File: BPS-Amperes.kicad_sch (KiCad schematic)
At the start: 37 parts, among them J1 Conn_02x10_Odd_Even, J2 ShuntConn, U1 INA186A3IDDFT, U2 OPA2196, U3 LTC2315, U4 REF1930AIDDCT

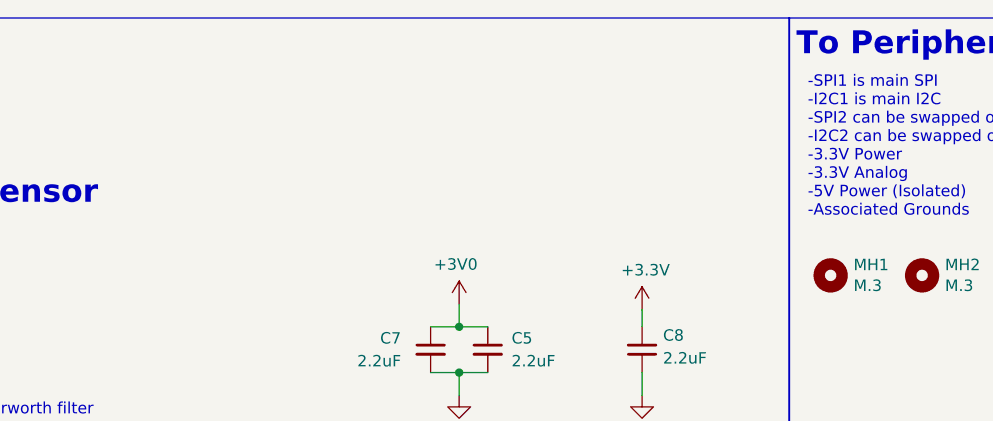
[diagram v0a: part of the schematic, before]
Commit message: Added Shunt Passthrough & Test Conns
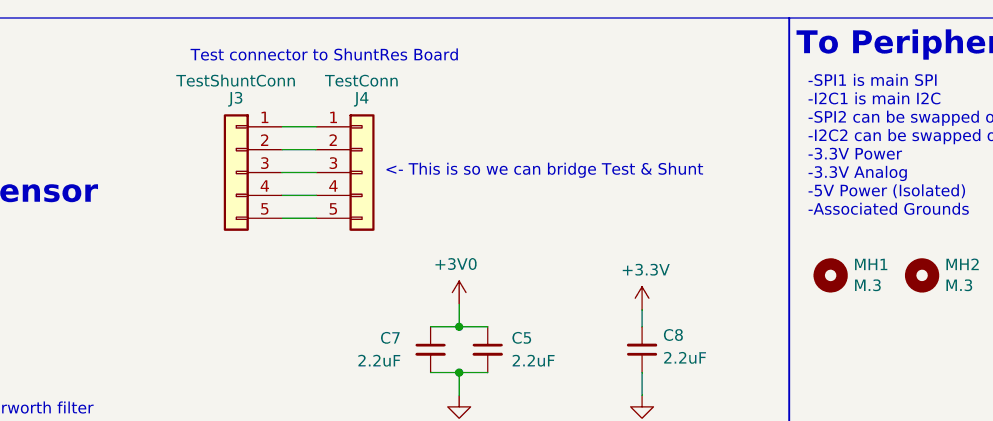
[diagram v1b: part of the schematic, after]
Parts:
- added J3: TestShuntConn, Connector_PinSocket_2.54mm:PinSocket_1x05_P2.54mm_Vertical, symbol Connector_Generic:Conn_01x05
- added J4: TestConn, Connector_PinSocket_2.54mm:PinSocket_1x05_P2.54mm_Horizontal, symbol Connector_Generic:Conn_01x05
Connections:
- new net: J3.1 (Pin_1), J4.1 (Pin_1)
- new net: J3.2 (Pin_2), J4.2 (Pin_2)
- new net: J3.3 (Pin_3), J4.3 (Pin_3)
- new net: J3.4 (Pin_4), J4.4 (Pin_4)
- new net: J3.5 (Pin_5), J4.5 (Pin_5)
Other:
- note added: "<- This is so we can bridge Test & Shunt"
- note added: "Test connector to ShuntRes Board"
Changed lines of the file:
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@@
+    (stroke (width 0) (type default))
+  )
+  (wire (pts (xy 120.65 26.67) (xy 124.46 26.67))
     (stroke (width 0) (type default))
   )
@@
     (stroke (width 0) (type default))
   )
+  (wire (pts (xy 120.65 31.75) (xy 124.46 31.75))
+    (stroke (width 0) (type default))
+  )
   (wire (pts (xy 122.555 78.74) (xy 123.825 78.74))
     (stroke (width 0) (type default))
@@
     (stroke (width 0) (type default))
   )
+  (wire (pts (xy 120.65 34.29) (xy 124.46 34.29))
+    (stroke (width 0) (type default))
+  )
   (wire (pts (xy 226.06 35.56) (xy 224.155 35.56))
     (stroke (width 0) (type default))
@@
     (stroke (width 0) (type default))
   )
+  (wire (pts (xy 120.65 24.13) (xy 124.46 24.13))
+    (stroke (width 0) (type default))
+  )
   (wire (pts (xy 238.125 30.48) (xy 241.3 30.48))
     (stroke (width 0) (type default))
@@
   )
   (wire (pts (xy 278.13 38.1) (xy 280.035 38.1))
+    (stroke (width 0) (type default))
+  )
+  (wire (pts (xy 120.65 29.21) (xy 124.46 29.21))
     (stroke (width 0) (type default))
   )
@@
   (text "To Peripheral SOM" (at 177.8 16.51 0)
     (effects (font (size 2.54 2.54) (thickness 0.508) bold) (justify left bottom))
+  )
+  (text "Test connector to ShuntRes Board" (at 110.49 17.145 0)
+    (effects (font (size 1.27 1.27)) (justify left bottom))
   )
   (text "Current shunt resistor (100u ohms) and thermistor (PT1000) will\nbe placed on a separate PCB located closer to the battery. "
@@
   (text "Daughterboard Features" (at 12.7 16.51 0)
     (effects (font (size 2.54 2.54) (thickness 0.508) bold) (justify left bottom))
+  )
+  (text "<- This is so we can bridge Test & Shunt" (at 132.08 29.845 0)
+    (effects (font (size 1.27 1.27)) (justify left bottom))
   )
   (text "-SPI1 is main SPI\n-I2C1 is main I2C\n-SPI2 can be swapped out for 4xGPIO\n-I2C2 can be swapped out for 2xGPIO\n-3.3V Power\n-3.3V Analog\n-5V Power (Isolated)\n-Associated Grounds"
@@
     )
   )
+  (symbol (lib_id "Connector_Generic:Conn_01x05") (at 129.54 29.21 0) (unit 1)
+    (in_bom yes) (on_board yes) (dnp no)
+    (property "Reference" "J4" (at 129.54 20.955 0)
+      (effects (font (size 1.27 1.27)))
+    )
+    (property "Value" "TestConn" (at 129.54 19.05 0)
+      (effects (font (size 1.27 1.27)))
+    )
+    (property "Footprint" "Connector_PinSocket_2.54mm:PinSocket_1x05_P2.54mm_Horizontal" (at 129.54 29.21 0)
+      (effects (font (size 1.27 1.27)) hide)
+    )
+    (property "Datasheet" "~" (at 129.54 29.21 0)
+      (effects (font (size 1.27 1.27)) hide)
+    )
+    (pin "1")
+    (pin "2")
+    (pin "3")
+    (pin "4")
+    (pin "5")
+    (instances
+      (project "BPS-Amperes"
+        (path "/637f68f0-cb9c-412a-8573-5d8e7ef6d8a2"
+          (reference "J4") (unit 1)
+        )
+      )
+      (project "BPS-Amperes"
+        (path "/e63e39d7-6ac0-4ffd-8aa3-1841a4541b55"
+          (reference "J1") (unit 1)
+        )
+      )
+    )
+  )
   (symbol (lib_id "Connector_Generic:Conn_01x05") (at 22.225 43.18 0) (mirror y) (unit 1)
     (in_bom yes) (on_board yes) (dnp no)
@@
         )
       )
+    )
+  )
+  (symbol (lib_id "Connector_Generic:Conn_01x05") (at 115.57 29.21 0) (mirror y) (unit 1)
+    (in_bom yes) (on_board yes) (dnp no)
+    (property "Reference" "J3" (at 115.57 20.955 0)
+      (effects (font (size 1.27 1.27)))
+    )
+    (property "Value" "TestShuntConn" (at 115.57 19.05 0)
+      (effects (font (size 1.27 1.27)))
+    )
+    (property "Footprint" "Connector_PinSocket_2.54mm:PinSocket_1x05_P2.54mm_Vertical" (at 115.57 29.21 0)
+      (effects (font (size 1.27 1.27)) hide)
+    )
+    (property "Datasheet" "~" (at 115.57 29.21 0)
+      (effects (font (size 1.27 1.27)) hide)
+    )
+    (pin "1")
+    (pin "2")
+    (pin "3")
+    (pin "4")
+    (pin "5")
+    (instances
+      (project "BPS-Amperes"
+        (path "/637f68f0-cb9c-412a-8573-5d8e7ef6d8a2"
+          (reference "J3") (unit 1)
+        )
+      )
+      (project "BPS-Amperes"
+        (path "/e63e39d7-6ac0-4ffd-8aa3-1841a4541b55"
+          (reference "J1") (unit 1)
+        )
+      )

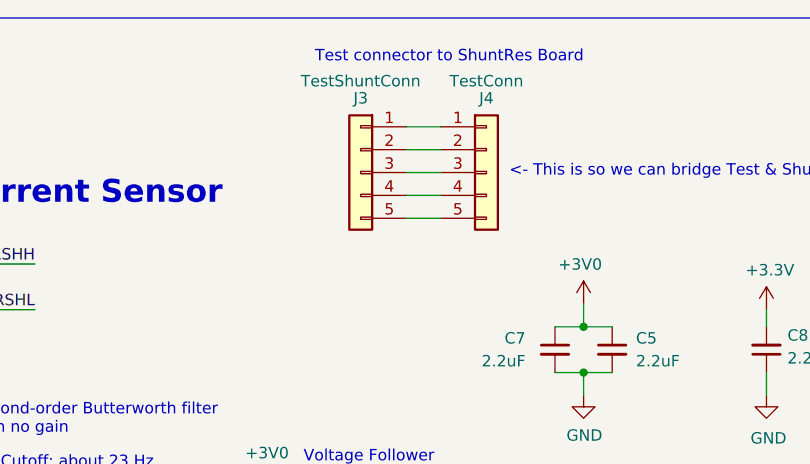
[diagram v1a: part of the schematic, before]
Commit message: Added Mounting Holes to RShunt Board
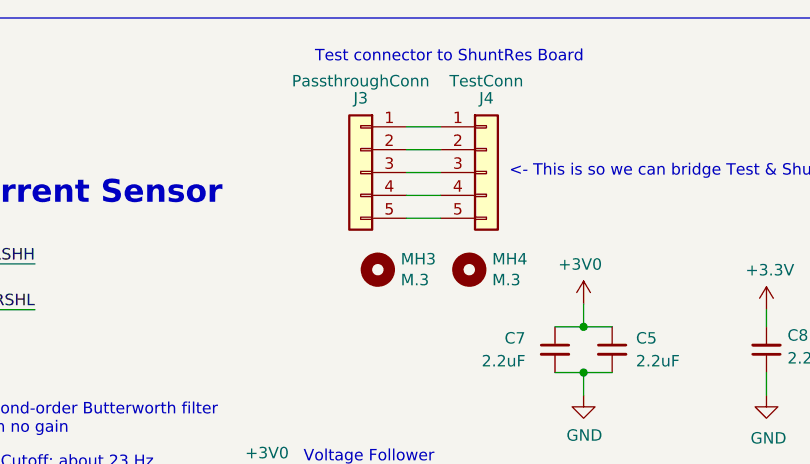
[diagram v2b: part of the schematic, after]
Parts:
- added MH3, MH4: M.3, MountingHole:MountingHole_2.7mm_M2.5, symbol Mechanical:MountingHole
- J3: value TestShuntConn -> PassthroughConn
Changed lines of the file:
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@@
+    )
+  )
+  (symbol (lib_id "Mechanical:MountingHole") (at 127.635 40.005 0) (unit 1)
+    (in_bom yes) (on_board yes) (dnp no)
+    (property "Reference" "MH4" (at 130.175 38.8366 0)
+      (effects (font (size 1.27 1.27)) (justify left))
+    )
+    (property "Value" "M.3" (at 130.175 41.148 0)
+      (effects (font (size 1.27 1.27)) (justify left))
+    )
+    (property "Footprint" "MountingHole:MountingHole_2.7mm_M2.5" (at 127.635 40.005 0)
+      (effects (font (size 1.27 1.27)) hide)
+    )
+    (property "Datasheet" "~" (at 127.635 40.005 0)
+      (effects (font (size 1.27 1.27)) hide)
+    )
+    (instances
+      (project "BPS-Amperes"
+        (path "/637f68f0-cb9c-412a-8573-5d8e7ef6d8a2"
+          (reference "MH4") (unit 1)
+        )
+      )
+      (project "BPS-Leader"
+        (path "/c248b171-df31-4e8a-afb6-607fa2df334b"
+          (reference "MH2") (unit 1)
+        )
+      )
+      (project "BPS-PeripheralSOM"
+        (path "/d5ebd247-5a7c-47c2-8aee-beabaef72d6d"
+          (reference "MH2") (unit 1)
+        )
+      )
     )
   )
@@
     )
   )
+  (symbol (lib_id "Mechanical:MountingHole") (at 117.475 40.005 0) (unit 1)
+    (in_bom yes) (on_board yes) (dnp no)
+    (property "Reference" "MH3" (at 120.015 38.8366 0)
+      (effects (font (size 1.27 1.27)) (justify left))
+    )
+    (property "Value" "M.3" (at 120.015 41.148 0)
+      (effects (font (size 1.27 1.27)) (justify left))
+    )
+    (property "Footprint" "MountingHole:MountingHole_2.7mm_M2.5" (at 117.475 40.005 0)
+      (effects (font (size 1.27 1.27)) hide)
+    )
+    (property "Datasheet" "~" (at 117.475 40.005 0)
+      (effects (font (size 1.27 1.27)) hide)
+    )
+    (instances
+      (project "BPS-Amperes"
+        (path "/637f68f0-cb9c-412a-8573-5d8e7ef6d8a2"
+          (reference "MH3") (unit 1)
+        )
+      )
+      (project "BPS-Leader"
+        (path "/c248b171-df31-4e8a-afb6-607fa2df334b"
+          (reference "MH1") (unit 1)
+        )
+      )
+      (project "BPS-PeripheralSOM"
+        (path "/d5ebd247-5a7c-47c2-8aee-beabaef72d6d"
+          (reference "MH1") (unit 1)
+        )
+      )
+    )
+  )
   (symbol (lib_id "Device:C_Small") (at 69.215 69.85 180) (unit 1)
     (in_bom yes) (on_board yes) (dnp no)
@@
       (effects (font (size 1.27 1.27)))
     )
-    (property "Value" "TestShuntConn" (at 115.57 19.05 0)
-      (effects (font (size 1.27 1.27)))
-    )
+    (property "Value" "PassthroughConn" (at 115.57 19.05 0)
+      (effects (font (size 1.27 1.27)))
+    )

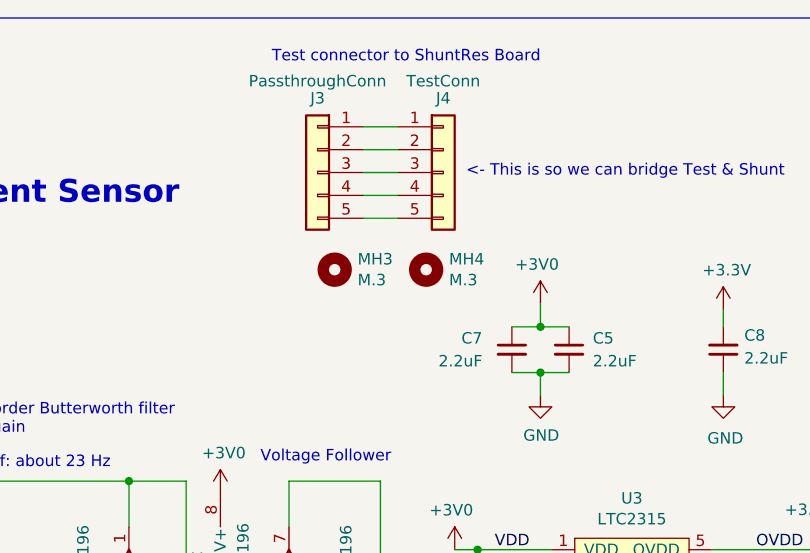
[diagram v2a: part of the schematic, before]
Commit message: Sike we don't need mounting holes
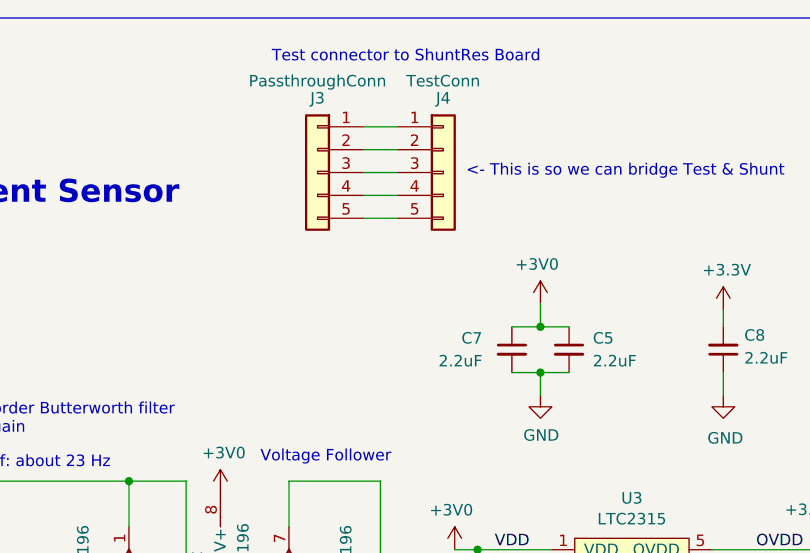
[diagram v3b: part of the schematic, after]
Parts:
- removed MH3, MH4: M.3, MountingHole:MountingHole_2.7mm_M2.5, symbol Mechanical:MountingHole
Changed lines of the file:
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@@
-    )
-  )
-  (symbol (lib_id "Mechanical:MountingHole") (at 127.635 40.005 0) (unit 1)
-    (in_bom yes) (on_board yes) (dnp no)
-    (property "Reference" "MH4" (at 130.175 38.8366 0)
-      (effects (font (size 1.27 1.27)) (justify left))
-    )
-    (property "Value" "M.3" (at 130.175 41.148 0)
-      (effects (font (size 1.27 1.27)) (justify left))
-    )
-    (property "Footprint" "MountingHole:MountingHole_2.7mm_M2.5" (at 127.635 40.005 0)
-      (effects (font (size 1.27 1.27)) hide)
-    )
-    (property "Datasheet" "~" (at 127.635 40.005 0)
-      (effects (font (size 1.27 1.27)) hide)
-    )
-    (instances
-      (project "BPS-Amperes"
-        (path "/637f68f0-cb9c-412a-8573-5d8e7ef6d8a2"
-          (reference "MH4") (unit 1)
-        )
-      )
-      (project "BPS-Leader"
-        (path "/c248b171-df31-4e8a-afb6-607fa2df334b"
-          (reference "MH2") (unit 1)
-        )
-      )
-      (project "BPS-PeripheralSOM"
-        (path "/d5ebd247-5a7c-47c2-8aee-beabaef72d6d"
-          (reference "MH2") (unit 1)
-        )
-      )
     )
   )
@@
         )
       )
-    )
-  )
-  (symbol (lib_id "Mechanical:MountingHole") (at 117.475 40.005 0) (unit 1)
-    (in_bom yes) (on_board yes) (dnp no)
-    (property "Reference" "MH3" (at 120.015 38.8366 0)
-      (effects (font (size 1.27 1.27)) (justify left))
-    )
-    (property "Value" "M.3" (at 120.015 41.148 0)
-      (effects (font (size 1.27 1.27)) (justify left))
-    )
-    (property "Footprint" "MountingHole:MountingHole_2.7mm_M2.5" (at 117.475 40.005 0)
-      (effects (font (size 1.27 1.27)) hide)
-    )
-    (property "Datasheet" "~" (at 117.475 40.005 0)
-      (effects (font (size 1.27 1.27)) hide)
-    )
-    (instances
-      (project "BPS-Amperes"
-        (path "/637f68f0-cb9c-412a-8573-5d8e7ef6d8a2"
-          (reference "MH3") (unit 1)
-        )
-      )
-      (project "BPS-Leader"
-        (path "/c248b171-df31-4e8a-afb6-607fa2df334b"
-          (reference "MH1") (unit 1)
-        )
-      )
-      (project "BPS-PeripheralSOM"
-        (path "/d5ebd247-5a7c-47c2-8aee-beabaef72d6d"
-          (reference "MH1") (unit 1)
-        )
-      )

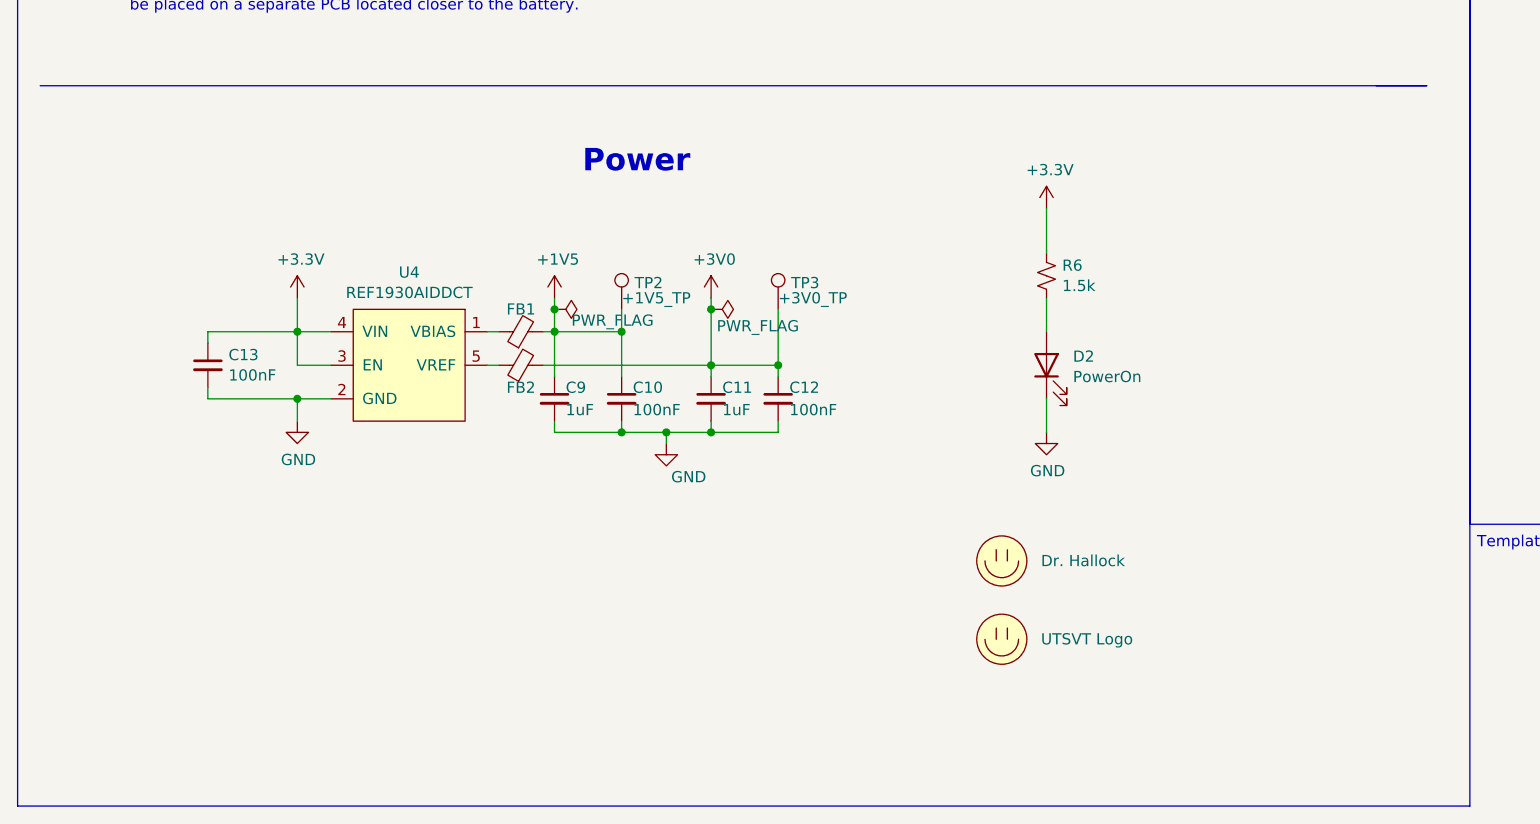
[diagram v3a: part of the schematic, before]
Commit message: Changed testpoints and arranged power components
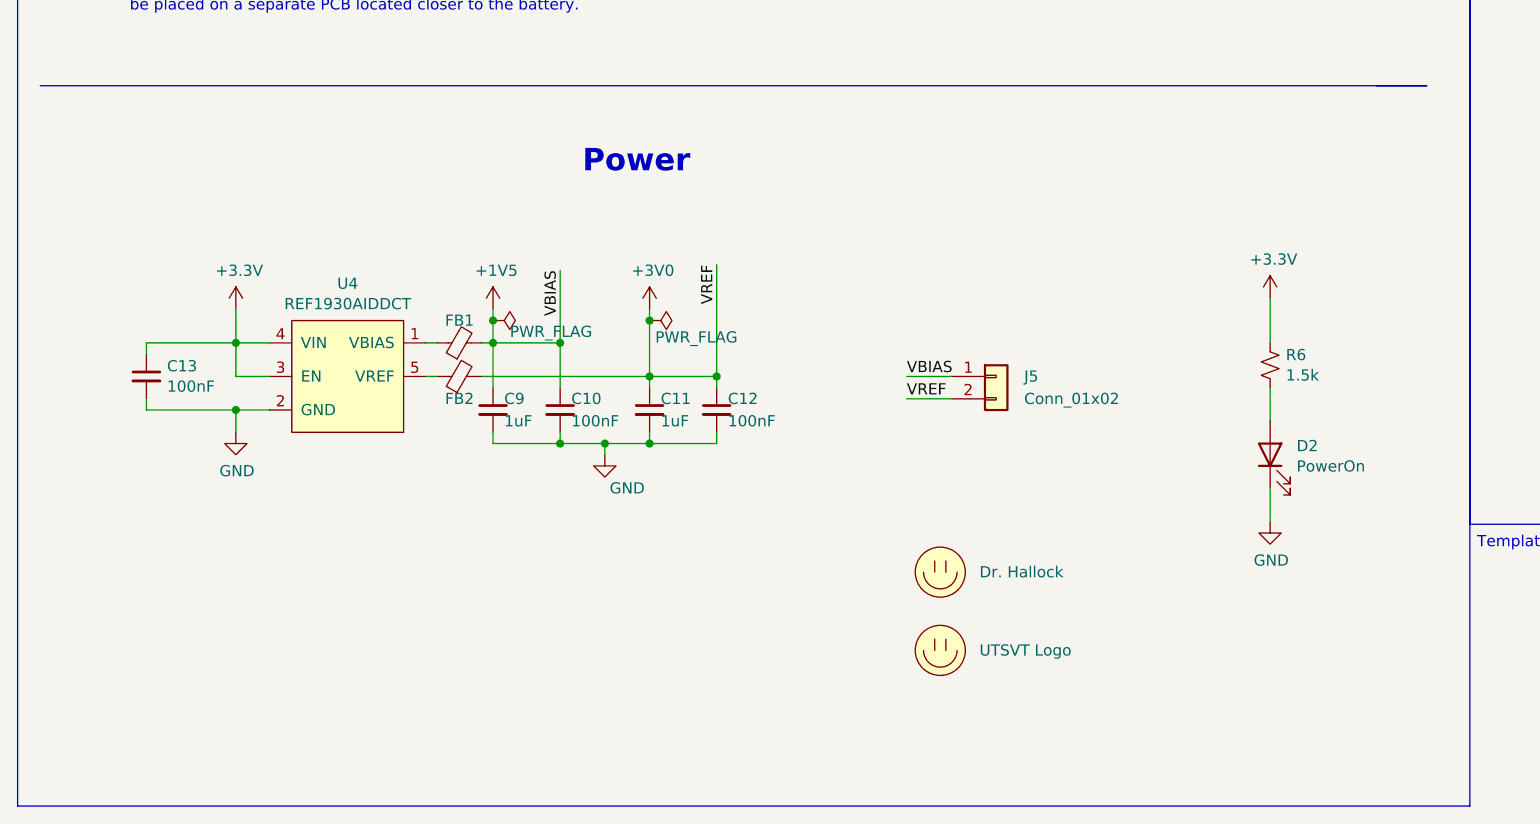
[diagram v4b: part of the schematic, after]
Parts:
- removed TP2: +1V5_TP, TestPoint:TestPoint_Pad_1.5x1.5mm, symbol Connector:TestPoint
- removed TP3: +3V0_TP, TestPoint:TestPoint_Pad_1.5x1.5mm, symbol Connector:TestPoint
- added J5: Conn_01x02, Connector_PinSocket_2.54mm:PinSocket_1x02_P2.54mm_Horizontal, symbol Connector_Generic:Conn_01x02
- TP1: footprint Connector_PinSocket_2.54mm:PinSocket_1x01_P2.54mm_Vertical -> Connector_PinSocket_2.54mm:PinSocket_1x01_P2.54mm_Horizontal
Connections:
- net +1V5: now also J5.1 (Pin_1)
- net +3V0: now also J5.2 (Pin_2)
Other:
- moved on the sheet: C10, C11, C12, C13, C9, D2, FB1, FB2, R6, U4

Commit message: Reworking first iteration v1
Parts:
- removed C8: 2.2uF, Capacitor_SMD:C_0805_2012Metric, symbol Device:C_Small
- removed R7: 49.9, Resistor_SMD:R_0805_2012Metric, symbol Device:R_Small_US
- removed U3: LTC2315, Package_TO_SOT_SMD:SOT-23-8, symbol utsvt-chips:LTC2315
- D1: value 3.0V±0.05 -> 3.3V±0.05
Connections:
- net GNDPWR is gone; now on net Aout: J1.20 (Pin_20)
- net Aout: now reaches C6.1, D1.1 (K), R5.2, TP1.1
- no-connect marks 12 -> 11

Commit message: fix broken layout
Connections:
- no-connect marks 11 -> 14
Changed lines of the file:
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@@
   (no_connect (at 238.76 27.94))
   (no_connect (at 238.76 25.4))
+  (no_connect (at 238.76 40.64))
   (no_connect (at 256.54 30.48))
   (no_connect (at 34.925 38.1))
@@
   (no_connect (at 256.54 33.02))
   (no_connect (at 238.125 33.02))
+  (no_connect (at 239.395 43.18))
   (no_connect (at 257.81 43.18))
+  (no_connect (at 239.395 48.26))
   (no_connect (at 257.81 45.72))
   (no_connect (at 239.395 45.72))
